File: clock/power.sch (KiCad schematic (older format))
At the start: 48 parts

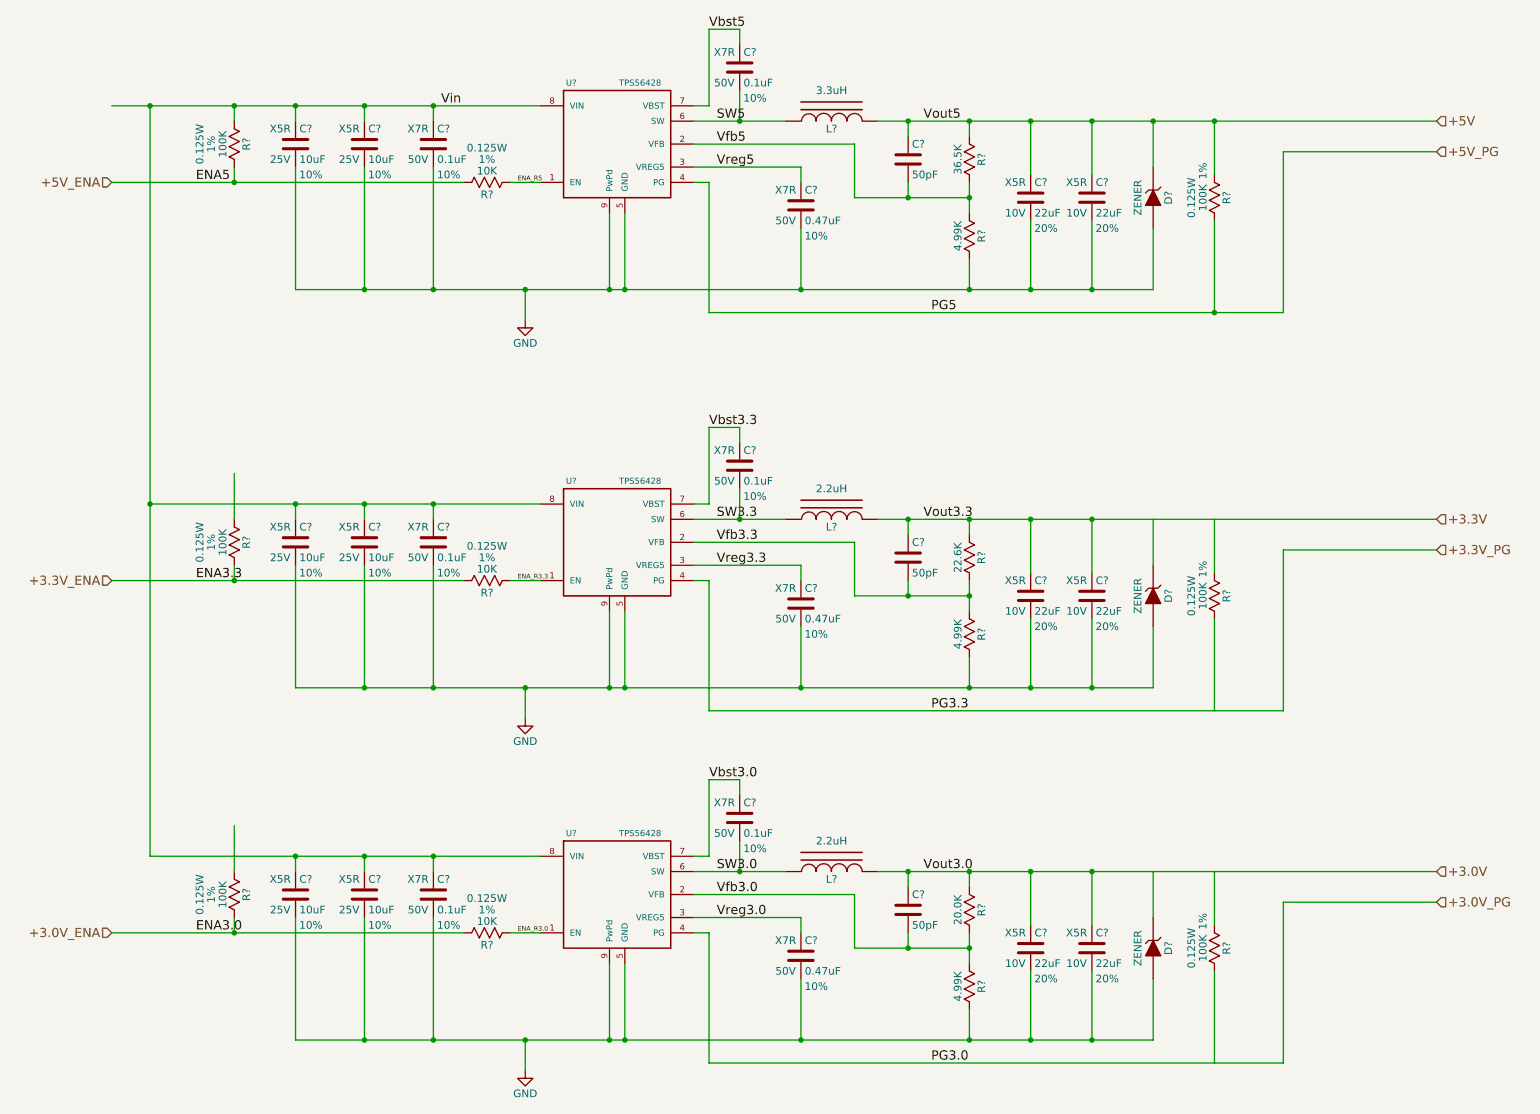
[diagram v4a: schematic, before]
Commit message: Fan and power connectors.
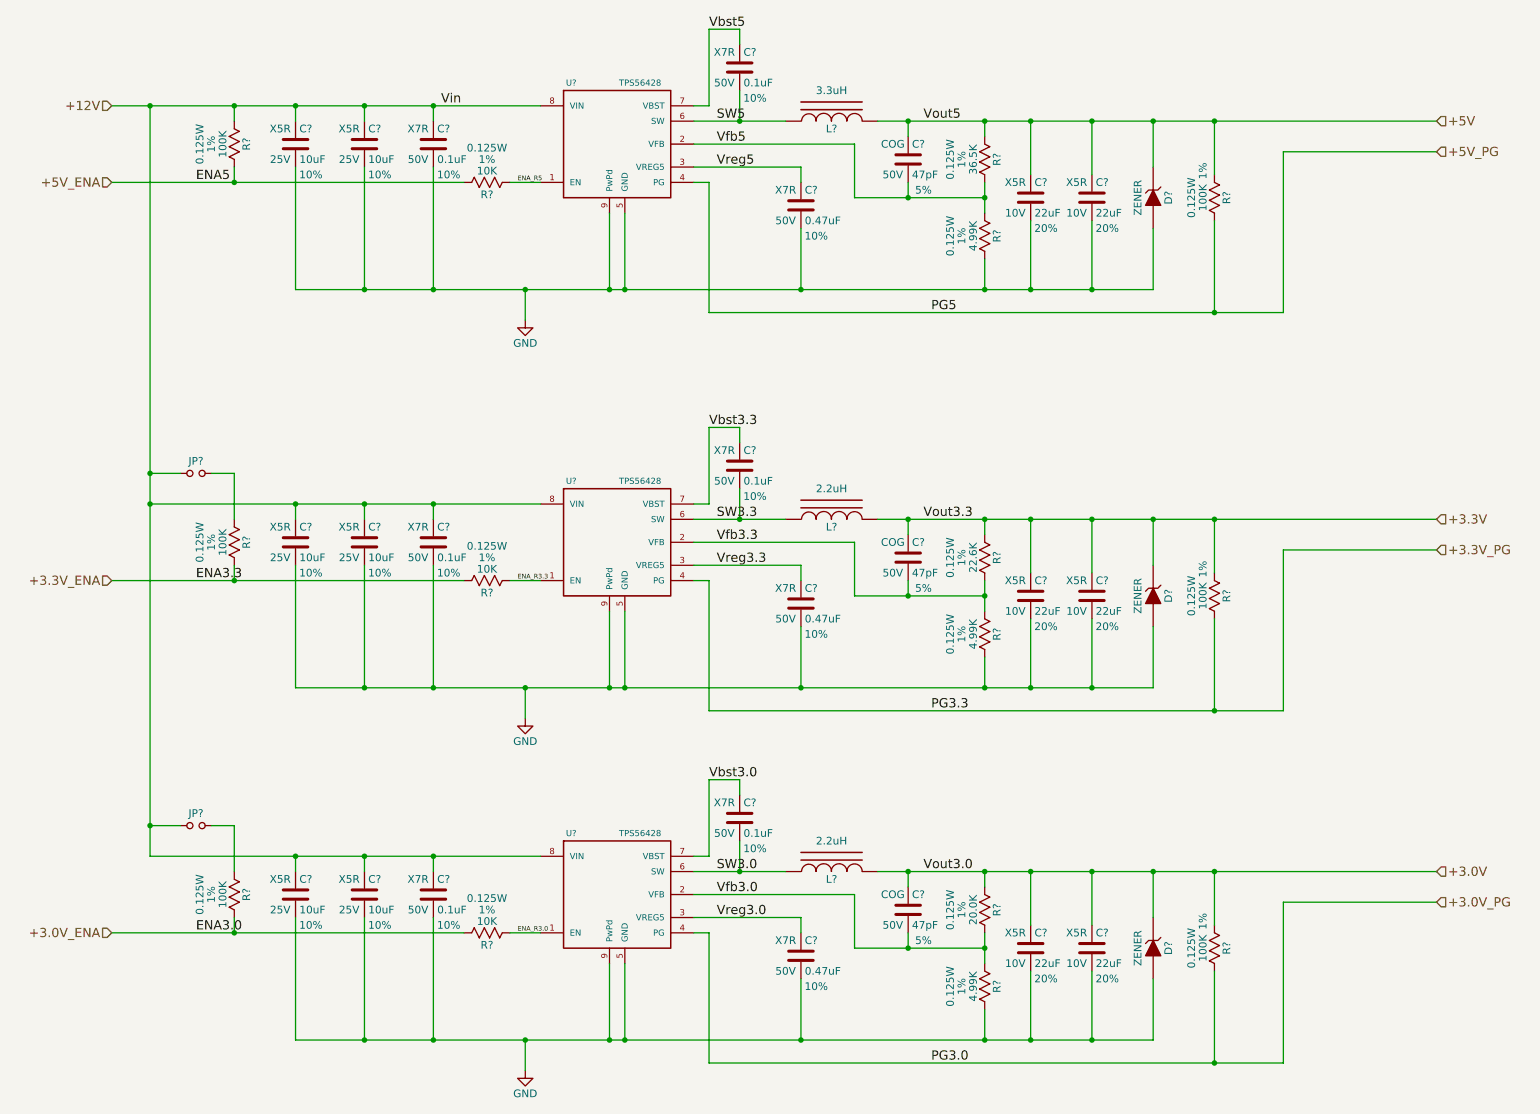
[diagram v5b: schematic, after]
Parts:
- removed C? (x3): 50pF, Capacitors_SMD:C_0805_HandSoldering, symbol C
- removed R? (x3): 4.99K, symbol R_local
- removed R?: 36.5K, symbol R_local
- removed R?: 22.6K, symbol R_local
- removed R?: 20.0K, symbol R_local
- added C? (x3): 47pF, Capacitors_SMD:C_0805_HandSoldering, symbol C
- added JP? (x2): Jumper_NO_Small, symbol Jumper_NO_Small
- added R? (x3): 4.99K, Resistors_SMD:R_0805_HandSoldering, symbol R_local
- added R?: 36.5K, Resistors_SMD:R_0805_HandSoldering, symbol R_local
- added R?: 22.6K, Resistors_SMD:R_0805_HandSoldering, symbol R_local
- added R?: 20.0K, Resistors_SMD:R_0805_HandSoldering, symbol R_local
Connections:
- net labels added: +12V
- wire segments 139 -> 143

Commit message: Correct footprint selection. Start pcb. Add BOM files.
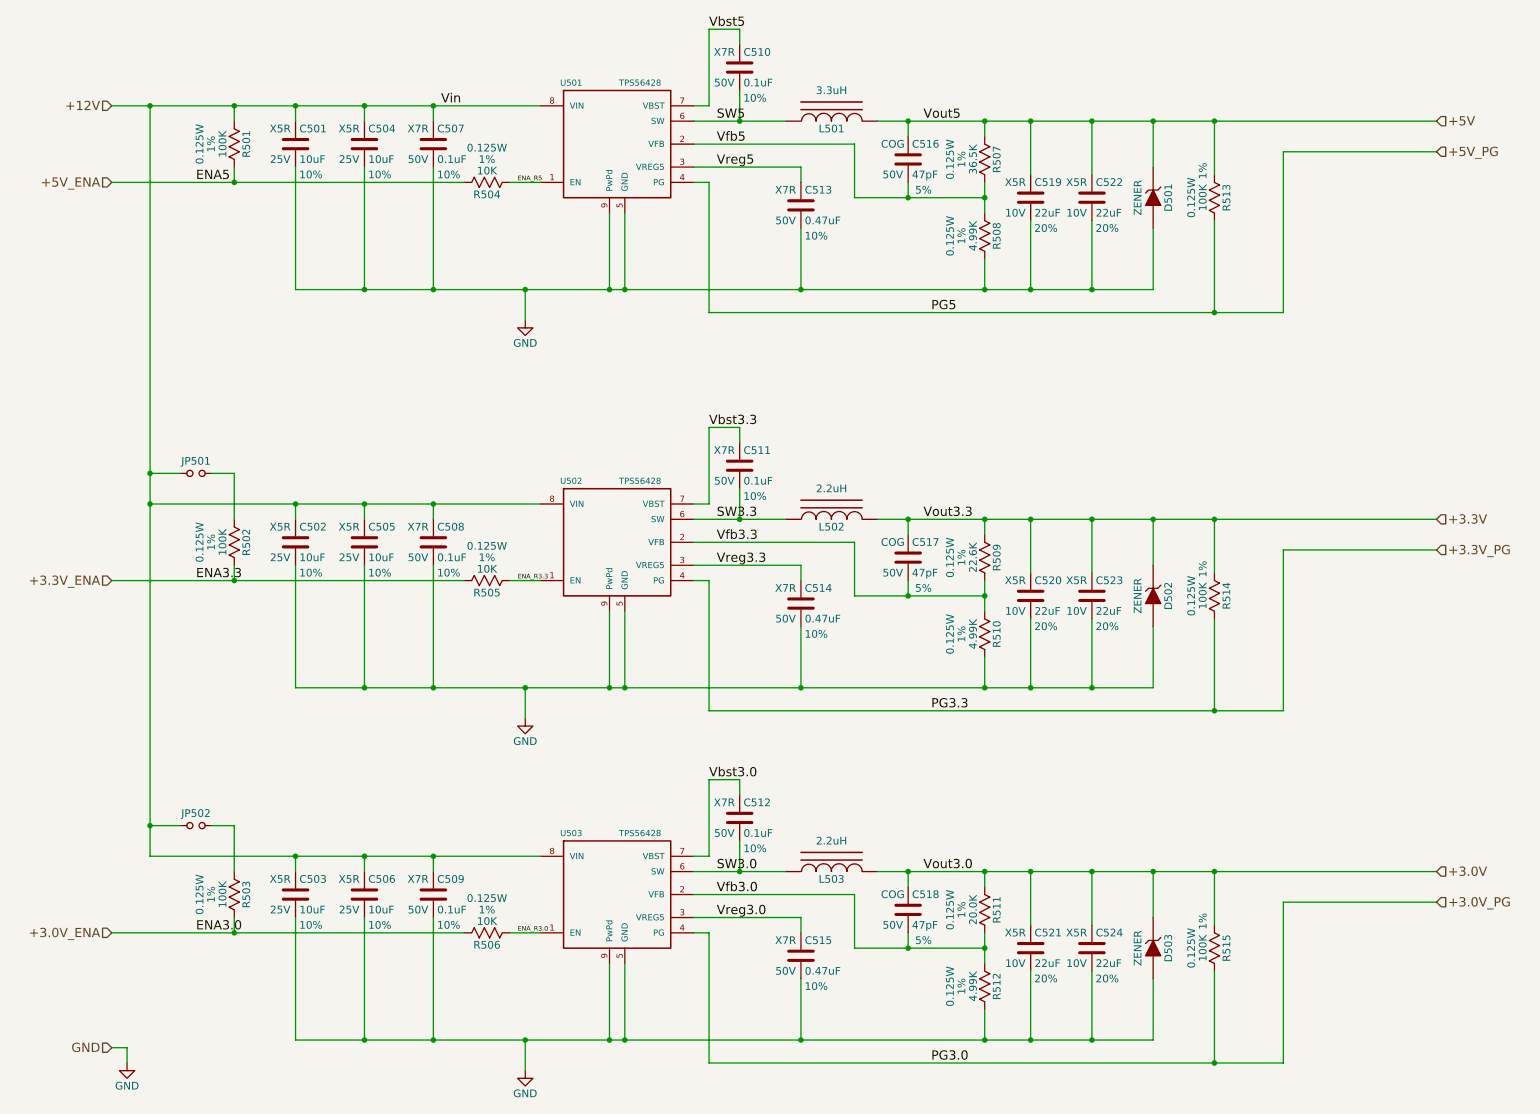
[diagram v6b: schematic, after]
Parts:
- D501, D502, D503: renamed from D?; footprint (none) -> Diodes_SMD:SOD-123
- JP501, JP502: renamed from JP?; footprint (none) -> Pin_Headers:Pin_Header_Straight_1x02
- U501, U502, U503: renamed from U?; footprint (none) -> local:SOIC-8_PowerPAD_HandSoldering
- gave numbers to parts that had none: 42

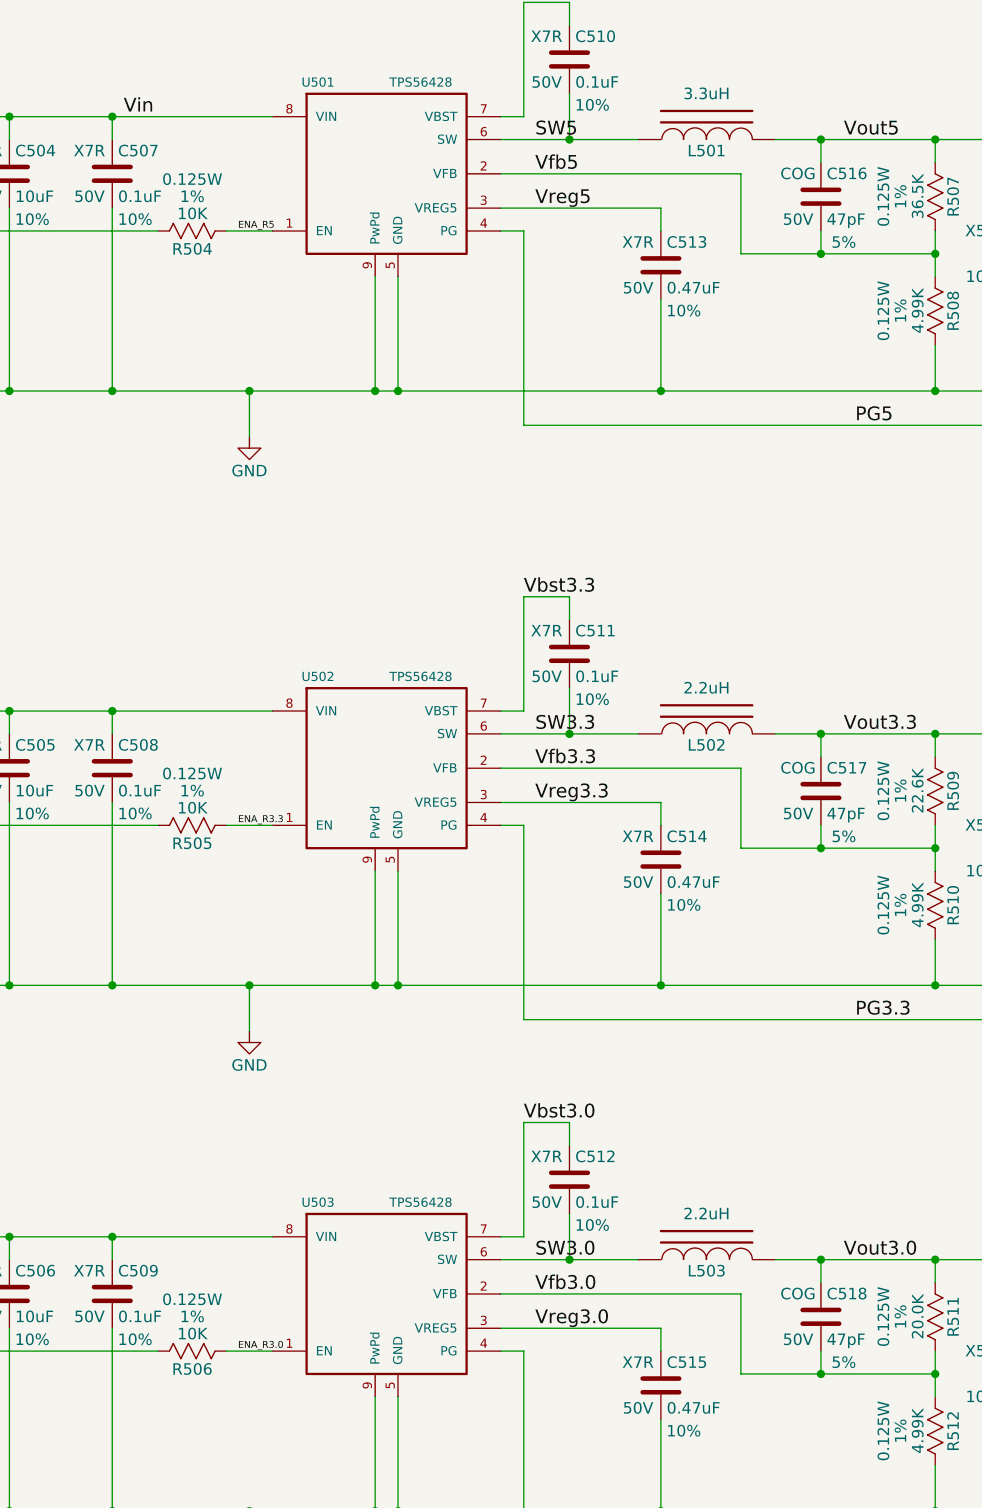
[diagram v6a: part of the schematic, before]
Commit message: Make component parameters consistent for BOM.
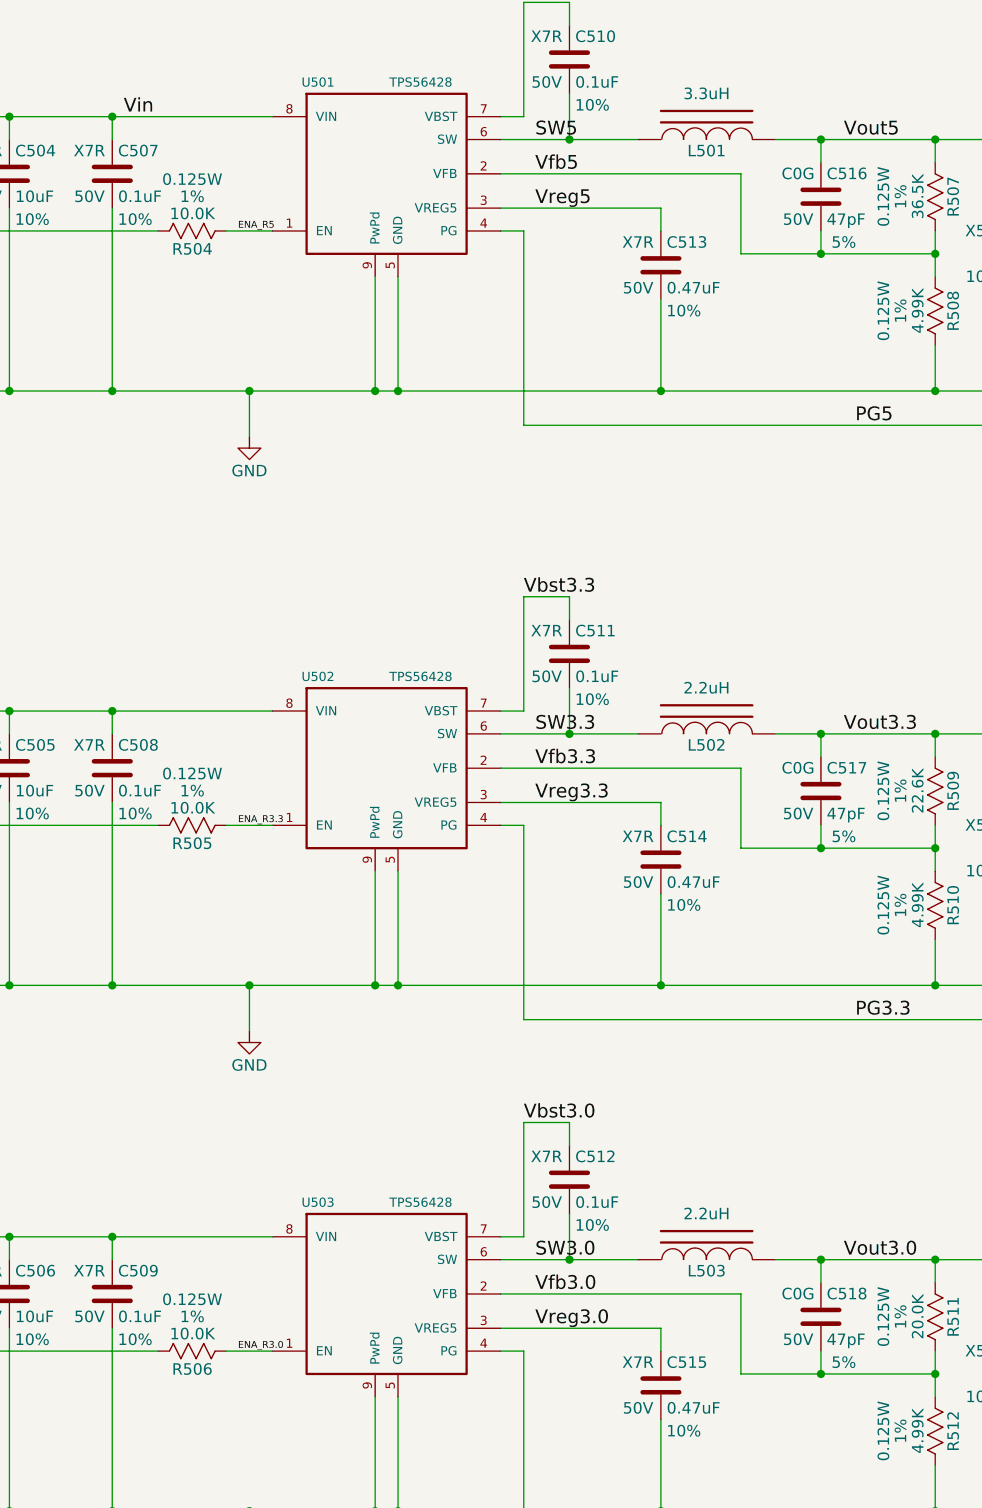
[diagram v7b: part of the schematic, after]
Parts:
- C516, C517, C518: Dielectric COG -> C0G
- R504, R505, R506: value 10K -> 10.0K
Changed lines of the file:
@@
 P 5950 2750
 F 0 "R504" V 6030 2750 50  0000 C CNN
-F 1 "10K" V 5875 2750 50  0000 C CNN
+F 1 "10.0K" V 5875 2750 50  0000 C CNN
 F 2 "Resistors_SMD:R_0805_HandSoldering" V 5880 2750 30  0001 C CNN
 F 3 "" V 6030 2750 30  0000 C CNN
@@
 P 5950 5350
 F 0 "R505" V 6030 5350 50  0000 C CNN
-F 1 "10K" V 5875 5350 50  0000 C CNN
+F 1 "10.0K" V 5875 5350 50  0000 C CNN
 F 2 "Resistors_SMD:R_0805_HandSoldering" V 5880 5350 30  0001 C CNN
 F 3 "" V 6030 5350 30  0000 C CNN
@@
 P 5950 7650
 F 0 "R506" V 6030 7650 50  0000 C CNN
-F 1 "10K" V 5875 7650 50  0000 C CNN
+F 1 "10.0K" V 5875 7650 50  0000 C CNN
 F 2 "Resistors_SMD:R_0805_HandSoldering" V 5880 7650 30  0001 C CNN
 F 3 "" V 6030 7650 30  0000 C CNN
@@
 F 4 "50V" H 8600 2500 50  0000 C CNN "Voltage"
 F 5 "5%" H 8800 2400 50  0000 C CNN "Tolerance"
-F 6 "COG" H 8600 2700 50  0000 C CNN "Dielectric"
+F 6 "C0G" H 8600 2700 50  0000 C CNN "Dielectric"
 F 7 "Kemet" H 8700 2600 50  0001 C CNN "Manufacturer"
 F 8 "C0805C470J5GACTU" H 8700 2600 50  0001 C CNN "PartNum"
@@
 F 4 "50V" H 8600 5100 50  0000 C CNN "Voltage"
 F 5 "5%" H 8800 5000 50  0000 C CNN "Tolerance"
-F 6 "COG" H 8600 5300 50  0000 C CNN "Dielectric"
+F 6 "C0G" H 8600 5300 50  0000 C CNN "Dielectric"
 F 7 "Kemet" H 8700 5200 50  0001 C CNN "Manufacturer"
 F 8 "C0805C470J5GACTU" H 8700 5200 50  0001 C CNN "PartNum"
@@
 F 4 "50V" H 8600 7400 50  0000 C CNN "Voltage"
 F 5 "5%" H 8800 7300 50  0000 C CNN "Tolerance"
-F 6 "COG" H 8600 7600 50  0000 C CNN "Dielectric"
+F 6 "C0G" H 8600 7600 50  0000 C CNN "Dielectric"
 F 7 "Kemet" H 8700 7500 50  0001 C CNN "Manufacturer"
 F 8 "C0805C470J5GACTU" H 8700 7500 50  0001 C CNN "PartNum"
